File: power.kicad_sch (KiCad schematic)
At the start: 27 parts, among them IC1 SiC437BED-T1-GE3, J4 Barrel_Jack_Switch, Q1 PXP012-30QLJ, Q2 PXP012-30QLJ, U2 LTC4412xS6

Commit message: with ports for steppers
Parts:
- IC1: footprint SiC437BEDT1GE3 -> iclr:SiC437BEDT1GE3
- Q1, Q2: footprint PXP01230QLJ -> iclr:PXP01230QLJ
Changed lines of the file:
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@@
 			)
 		)
-		(property "Footprint" "PXP01230QLJ"
+		(property "Footprint" "iclr:PXP01230QLJ"
 			(at 96.52 88.9 0)
 			(effects
@@
 			)
 		)
-		(property "Footprint" "SiC437BEDT1GE3"
+		(property "Footprint" "iclr:SiC437BEDT1GE3"
 			(at 187.96 35.56 0)
 			(effects
@@
 			)
 		)
-		(property "Footprint" "PXP01230QLJ"
+		(property "Footprint" "iclr:PXP01230QLJ"
 			(at 81.28 21.59 0)
 			(effects

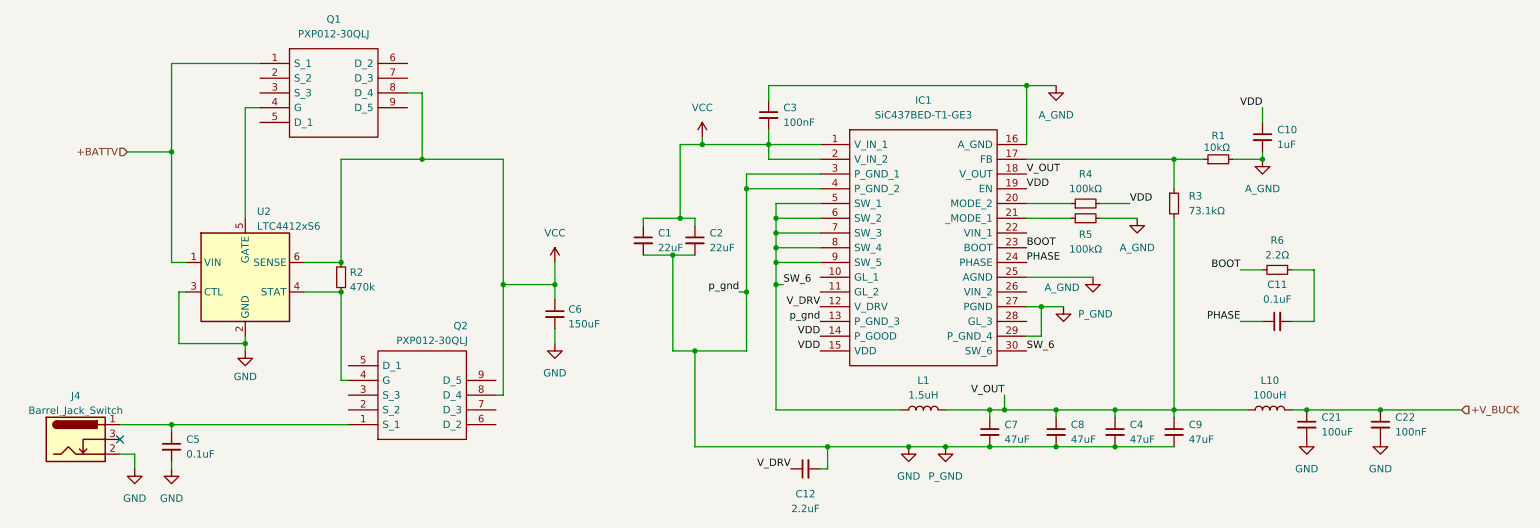
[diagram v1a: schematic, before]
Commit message: added zener diodes
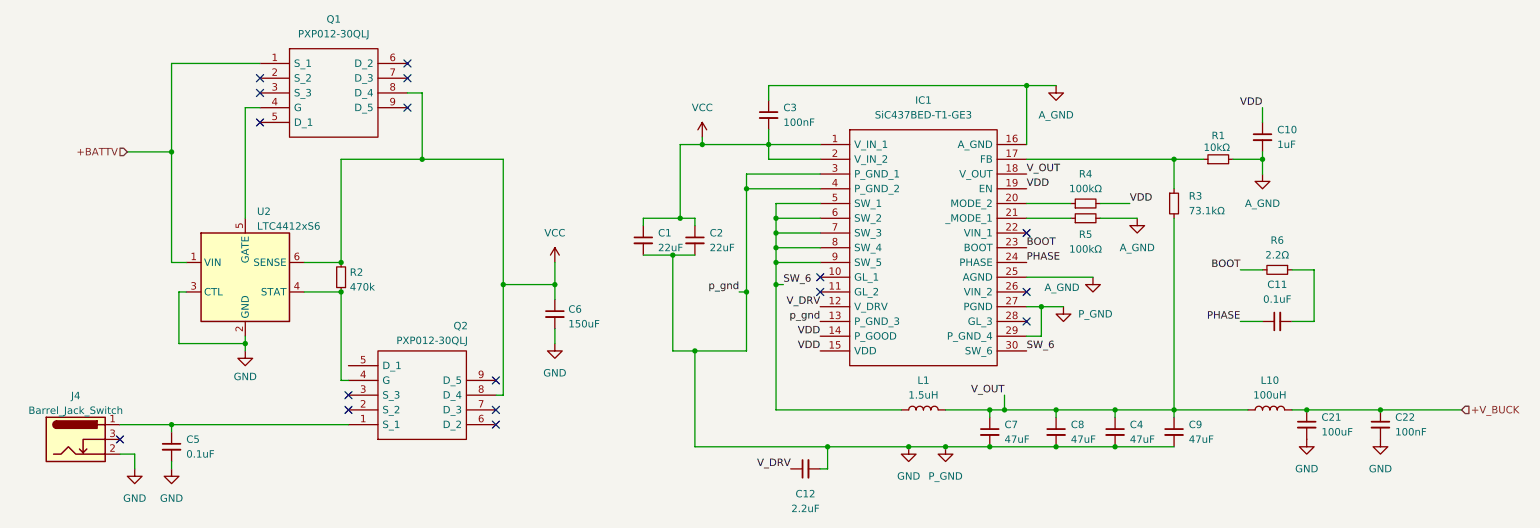
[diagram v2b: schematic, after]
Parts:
- C1, C2: footprint (none) -> Capacitor_SMD:C_0805_2012Metric
- C10, C12: footprint (none) -> Capacitor_SMD:C_0603_1608Metric
- C11, C22, C3: footprint (none) -> Capacitor_SMD:C_0402_1005Metric
- C21: footprint (none) -> Capacitor_SMD:C_Elec_6.3x5.4
- C4, C7, C8, C9: footprint (none) -> Capacitor_SMD:C_1206_3216Metric
- C5: footprint Capacitor_SMD:C_0603_1608Metric -> Capacitor_SMD:C_0402_1005Metric
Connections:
- no-connect marks 1 -> 17
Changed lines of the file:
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@@
 	)
 	(no_connect
+		(at 85.09 31.75)
+	)
+	(no_connect
+		(at 59.69 29.21)
+	)
+	(no_connect
+		(at 74.93 83.82)
+	)
+	(no_connect
+		(at 191.77 53.34)
+	)
+	(no_connect
+		(at 191.77 63.5)
+	)
+	(no_connect
 		(at 35.56 88.9)
 	)
+	(no_connect
+		(at 156.21 60.96)
+	)
+	(no_connect
+		(at 156.21 63.5)
+	)
+	(no_connect
+		(at 59.69 26.67)
+	)
+	(no_connect
+		(at 100.33 86.36)
+	)
+	(no_connect
+		(at 100.33 78.74)
+	)
+	(no_connect
+		(at 191.77 68.58)
+	)
+	(no_connect
+		(at 74.93 81.28)
+	)
+	(no_connect
+		(at 85.09 26.67)
+	)
+	(no_connect
+		(at 85.09 24.13)
+	)
+	(no_connect
+		(at 59.69 34.29)
+	)
+	(no_connect
+		(at 100.33 83.82)
+	)
 	(wire
 		(pts
@@
 	(wire
 		(pts
+			(xy 232.41 43.18) (xy 232.41 40.64)
+		)
+		(stroke
+			(width 0)
+			(type default)
+		)
+	)
+	(wire
+		(pts
 			(xy 148.59 58.42) (xy 148.59 62.23)
 		)
@@
 			)
 		)
-		(property "Footprint" ""
+		(property "Footprint" "Capacitor_SMD:C_Elec_6.3x5.4"
 			(at 240.03 86.36 0)
 			(effects
@@
 			)
 		)
-		(property "Footprint" ""
+		(property "Footprint" "Capacitor_SMD:C_0402_1005Metric"
 			(at 234.95 68.58 0)
 			(effects
@@
 			)
 		)
-		(property "Footprint" ""
+		(property "Footprint" "Capacitor_SMD:C_0603_1608Metric"
 			(at 153.67 93.98 0)
 			(effects
@@
 			)
 		)
-		(property "Footprint" ""
+		(property "Footprint" "Capacitor_SMD:C_1206_3216Metric"
 			(at 185.42 87.63 0)
 			(effects
@@
 			)
 		)
-		(property "Footprint" ""
+		(property "Footprint" "Capacitor_SMD:C_0805_2012Metric"
 			(at 125.73 54.61 0)
 			(effects
@@
 			)
 		)
-		(property "Footprint" ""
+		(property "Footprint" "Capacitor_SMD:C_0805_2012Metric"
 			(at 134.62 54.61 0)
 			(effects
@@
 			)
 		)
-		(property "Footprint" ""
+		(property "Footprint" "Capacitor_SMD:C_1206_3216Metric"
 			(at 207.01 87.63 0)
 			(effects
@@
 			)
 		)
-		(property "Footprint" ""
+		(property "Footprint" "Capacitor_SMD:C_0603_1608Metric"
 			(at 232.41 36.83 0)
 			(effects
@@
 			)
 		)
-		(property "Footprint" ""
+		(property "Footprint" "Capacitor_SMD:C_1206_3216Metric"
 			(at 217.17 87.63 0)
 			(effects
@@
 			)
 		)
-		(property "Footprint" ""
+		(property "Footprint" "Capacitor_SMD:C_1206_3216Metric"
 			(at 196.85 87.63 0)
 			(effects
@@
 			)
 		)
-		(property "Footprint" "Capacitor_SMD:C_0603_1608Metric"
+		(property "Footprint" "Capacitor_SMD:C_0402_1005Metric"
 			(at 44.45 90.17 0)
 			(effects
@@
 	(symbol
 		(lib_id "power:GND")
-		(at 232.41 40.64 0)
+		(at 232.41 43.18 0)
 		(unit 1)
 		(exclude_from_sim no)
@@
 		(fields_autoplaced yes)
 		(property "Reference" "#PWR06"
-			(at 232.41 46.99 0)
+			(at 232.41 49.53 0)
 			(effects
 				(font
@@
 		)
 		(property "Value" "A_GND"
-			(at 232.41 45.72 0)
+			(at 232.41 48.26 0)
 			(effects
 				(font
@@
 		)
 		(property "Footprint" ""
-			(at 232.41 40.64 0)
+			(at 232.41 43.18 0)
 			(effects
 				(font
@@
 		)
 		(property "Datasheet" ""
-			(at 232.41 40.64 0)
+			(at 232.41 43.18 0)
 			(effects
 				(font
@@
 		)
 		(property "Description" "Power symbol creates a global label with name \"GND\" , ground"
-			(at 232.41 40.64 0)
+			(at 232.41 43.18 0)
 			(effects
 				(font
@@
 			)
 		)
-		(property "Footprint" ""
+		(property "Footprint" "Capacitor_SMD:C_0402_1005Metric"
 			(at 147.32 33.02 0)
 			(effects
@@
 			)
 		)
-		(property "Footprint" ""
+		(property "Footprint" "Capacitor_SMD:C_0402_1005Metric"
 			(at 252.73 86.36 0)
 			(effects

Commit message: UPDATE
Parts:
- L1: footprint (none) -> Inductor_SMD:L_1008_2520Metric
- L10: footprint (none) -> iclr:SDR1307A101K
- R1: footprint (none) -> Resistor_SMD:R_0805_2012Metric
- R3: value 73.1kΩ -> 73.2kΩ; footprint (none) -> iclr:ERJHP6D1000V
- R4, R5: footprint (none) -> Resistor_SMD:R_2010_5025Metric_Pad1.40x2.65mm_HandSolder
- R6: footprint (none) -> Resistor_SMD:R_0603_1608Metric_Pad0.98x0.95mm_HandSolder
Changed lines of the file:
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@@
 			)
 		)
-		(property "Footprint" ""
+		(property "Footprint" "Resistor_SMD:R_0805_2012Metric"
 			(at 224.79 40.64 0)
 			(effects
@@
 			)
 		)
-		(property "Footprint" ""
+		(property "Footprint" "Resistor_SMD:R_0603_1608Metric_Pad0.98x0.95mm_HandSolder"
 			(at 234.95 59.69 0)
 			(effects
@@
 			)
 		)
-		(property "Footprint" ""
+		(property "Footprint" "Inductor_SMD:L_1008_2520Metric"
 			(at 173.99 83.82 0)
 			(effects
@@
 			)
 		)
-		(property "Value" "73.1kΩ"
+		(property "Value" "73.2kΩ"
 			(at 219.71 49.5299 0)
 			(effects
@@
 			)
 		)
-		(property "Footprint" ""
+		(property "Footprint" "iclr:ERJHP6D1000V"
 			(at 217.17 48.26 0)
 			(effects
@@
 			)
 		)
-		(property "Footprint" ""
+		(property "Footprint" "Resistor_SMD:R_2010_5025Metric_Pad1.40x2.65mm_HandSolder"
 			(at 201.93 50.8 0)
 			(effects
@@
 			)
 		)
-		(property "Footprint" ""
+		(property "Footprint" "Resistor_SMD:R_2010_5025Metric_Pad1.40x2.65mm_HandSolder"
 			(at 201.93 48.26 0)
 			(effects
@@
 			)
 		)
-		(property "Footprint" ""
+		(property "Footprint" "iclr:SDR1307A101K"
 			(at 233.68 83.82 0)
 			(effects

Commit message: update 2 everything is fixed
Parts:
- R4, R5: footprint Resistor_SMD:R_2010_5025Metric_Pad1.40x2.65mm_HandSolder -> Resistor_SMD:R_0402_1005Metric
- R6: footprint Resistor_SMD:R_0603_1608Metric_Pad0.98x0.95mm_HandSolder -> Resistor_SMD:R_0402_1005Metric
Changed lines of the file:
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@@
 			)
 		)
-		(property "Footprint" "Resistor_SMD:R_0603_1608Metric_Pad0.98x0.95mm_HandSolder"
+		(property "Footprint" "Resistor_SMD:R_0402_1005Metric"
 			(at 234.95 59.69 0)
 			(effects
@@
 			)
 		)
-		(property "Footprint" "Resistor_SMD:R_2010_5025Metric_Pad1.40x2.65mm_HandSolder"
+		(property "Footprint" "Resistor_SMD:R_0402_1005Metric"
 			(at 201.93 50.8 0)
 			(effects
@@
 			)
 		)
-		(property "Footprint" "Resistor_SMD:R_2010_5025Metric_Pad1.40x2.65mm_HandSolder"
+		(property "Footprint" "Resistor_SMD:R_0402_1005Metric"
 			(at 201.93 48.26 0)
 			(effects

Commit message: ideal diode update to be checked
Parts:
- removed J4: Barrel_Jack_Switch, Connector_BarrelJack:BarrelJack_Wuerth_6941xx301002, symbol Connector:Barrel_Jack_Switch
- added J3: XT60PW-M, iclr:AMASS_XT60PW-M, symbol ICLR:XT60PW-M
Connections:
- net +BATTV: now also C5.1, Q2.1 (S_1), J3.1 (+)
- net GND: now also J3.2 (-)
- no-connect marks 17 -> 16
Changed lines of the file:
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@@
 	)
 	(junction
+		(at 44.45 58.42)
+		(diameter 0)
+		(color 0 0 0 0)
+	)
+	(junction
 		(at 196.85 90.17)
 		(diameter 0)
@@
 	)
 	(no_connect
-		(at 35.56 88.9)
-	)
-	(no_connect
 		(at 156.21 60.96)
 	)
@@
 	(wire
 		(pts
+			(xy 44.45 58.42) (xy 44.45 86.36)
+		)
+		(stroke
+			(width 0)
+			(type default)
+		)
+	)
+	(wire
+		(pts
 			(xy 67.31 63.5) (xy 73.66 63.5)
 		)
@@
 	(wire
 		(pts
-			(xy 57.15 71.12) (xy 57.15 72.39)
+			(xy 34.29 87.63) (xy 34.29 86.36)
 		)
 		(stroke
@@
 	(wire
 		(pts
-			(xy 191.77 66.04) (xy 194.31 66.04)
+			(xy 57.15 71.12) (xy 57.15 72.39)
 		)
 		(stroke
@@
 	(wire
 		(pts
-			(xy 217.17 85.09) (xy 217.17 83.82)
+			(xy 191.77 66.04) (xy 194.31 66.04)
 		)
 		(stroke
@@
 	(wire
 		(pts
-			(xy 46.99 63.5) (xy 45.72 63.5)
+			(xy 34.29 90.17) (xy 34.29 91.44)
 		)
 		(stroke
@@
 	(wire
 		(pts
-			(xy 101.6 81.28) (xy 101.6 62.23)
+			(xy 217.17 85.09) (xy 217.17 83.82)
 		)
 		(stroke
@@
 	(wire
 		(pts
-			(xy 148.59 50.8) (xy 148.59 53.34)
+			(xy 101.6 81.28) (xy 101.6 62.23)
 		)
 		(stroke
@@
 	(wire
 		(pts
-			(xy 35.56 91.44) (xy 38.1 91.44)
+			(xy 148.59 50.8) (xy 148.59 53.34)
 		)
 		(stroke
@@
 	(wire
 		(pts
-			(xy 45.72 63.5) (xy 45.72 72.39)
+			(xy 46.99 63.5) (xy 46.99 72.39)
 		)
 		(stroke
@@
 	(wire
 		(pts
-			(xy 44.45 58.42) (xy 46.99 58.42)
+			(xy 187.96 83.82) (xy 196.85 83.82)
 		)
 		(stroke
@@
 	(wire
 		(pts
-			(xy 187.96 83.82) (xy 196.85 83.82)
+			(xy 241.3 68.58) (xy 241.3 59.69)
 		)
 		(stroke
@@
 	(wire
 		(pts
-			(xy 241.3 68.58) (xy 241.3 59.69)
+			(xy 185.42 90.17) (xy 196.85 90.17)
 		)
 		(stroke
@@
 	(wire
 		(pts
-			(xy 185.42 90.17) (xy 196.85 90.17)
+			(xy 147.32 35.56) (xy 147.32 38.1)
 		)
 		(stroke
@@
 	(wire
 		(pts
-			(xy 147.32 35.56) (xy 147.32 38.1)
+			(xy 143.51 63.5) (xy 143.51 73.66)
 		)
 		(stroke
@@
 	(wire
 		(pts
-			(xy 143.51 63.5) (xy 143.51 73.66)
+			(xy 67.31 58.42) (xy 73.66 58.42)
 		)
 		(stroke
@@
 	(wire
 		(pts
-			(xy 67.31 58.42) (xy 73.66 58.42)
+			(xy 34.29 86.36) (xy 44.45 86.36)
 		)
 		(stroke
@@
 	(wire
 		(pts
+			(xy 44.45 58.42) (xy 46.99 58.42)
+		)
+		(stroke
+			(width 0)
+			(type default)
+		)
+	)
+	(wire
+		(pts
 			(xy 87.63 40.64) (xy 101.6 40.64)
 		)
@@
 	(wire
 		(pts
-			(xy 45.72 72.39) (xy 57.15 72.39)
+			(xy 46.99 72.39) (xy 57.15 72.39)
 		)
 		(stroke
@@
 	(wire
 		(pts
-			(xy 35.56 86.36) (xy 44.45 86.36)
-		)
-		(stroke
-			(width 0)
-			(type default)
-		)
-	)
-	(wire
-		(pts
 			(xy 143.51 45.72) (xy 143.51 63.5)
 		)
@@
 	(wire
 		(pts
+			(xy 34.29 91.44) (xy 38.1 91.44)
+		)
+		(stroke
+			(width 0)
+			(type default)
+		)
+	)
+	(wire
+		(pts
 			(xy 132.08 50.8) (xy 132.08 38.1)
 		)
@@
 	)
 	(symbol
-		(lib_id "Connector:Barrel_Jack_Switch")
-		(at 27.94 88.9 0)
-		(unit 1)
-		(exclude_from_sim no)
-		(in_bom yes)
-		(on_board yes)
-		(dnp no)
-		(property "Reference" "J4"
-			(at 27.94 81.3902 0)
-			(effects
-				(font
-					(size 1.27 1.27)
-				)
-			)
-		)
-		(property "Value" "Barrel_Jack_Switch"
-			(at 27.94 83.9271 0)
-			(effects
-				(font
-					(size 1.27 1.27)
-				)
-			)
-		)
-		(property "Footprint" "Connector_BarrelJack:BarrelJack_Wuerth_6941xx301002"
-			(at 29.21 89.916 0)
-			(effects
-				(font
-					(size 1.27 1.27)
-				)
-				(hide yes)
-			)
-		)
-		(property "Datasheet" "~"
-			(at 29.21 89.916 0)
-			(effects
-				(font
-					(size 1.27 1.27)
-				)
-				(hide yes)
-			)
-		)
-		(property "Description" ""
-			(at 27.94 88.9 0)
-			(effects
-				(font
-					(size 1.27 1.27)
-				)
-				(hide yes)
-			)
-		)
-		(pin "1"
-		)
-		(pin "2"
-		)
-		(pin "3"
-		)
-		(instances
-			(project "BetetrDom"
-				(path "/3d73b00f-865e-402b-88ef-ae22e0a8ba36/837d0d5a-cb41-4001-b9fc-855d4a9018ff"
-					(reference "J4")
-					(unit 1)
-				)
-			)
-		)
-	)
-	(symbol
 		(lib_id "power:VCC")
 		(at 110.49 58.42 0)
@@
 					(unit 1)
 				)
+			)
+		)
+	)
+	(symbol
+		(lib_id "ICLR:XT60PW-M")
+		(at 24.13 90.17 0)
+		(mirror y)
+		(unit 1)
+		(exclude_from_sim no)
+		(in_bom yes)
+		(on_board yes)
+		(dnp no)
+		(property "Reference" "J3"
+			(at 24.13 97.79 0)
+			(effects
+				(font
+					(size 1.27 1.27)
+				)
+			)
+		)
+		(property "Value" "XT60PW-M"
+			(at 24.13 95.25 0)
+			(effects
+				(font
+					(size 1.27 1.27)
+				)
+			)
+		)
+		(property "Footprint" "iclr:AMASS_XT60PW-M"
+			(at 24.13 90.17 0)
+			(effects
+				(font
+					(size 1.27 1.27)
+				)
+				(justify bottom)
+				(hide yes)
+			)
+		)
+		(property "Datasheet" ""
+			(at 24.13 90.17 0)
+			(effects
+				(font
+					(size 1.27 1.27)
+				)
+				(hide yes)
+			)
+		)
+		(property "Description" ""
+			(at 24.13 90.17 0)
+			(effects
+				(font
+					(size 1.27 1.27)
+				)
+				(hide yes)
+			)
+		)
+		(property "STANDARD" "Manufacturer recommendations"
+			(at 24.13 90.17 0)
+			(effects
+				(font
+					(size 1.27 1.27)
+				)
+				(justify bottom)
+				(hide yes)
+			)
+		)
+		(property "MANUFACTURER" "AMASS"
+			(at 24.13 90.17 0)
+			(effects
+				(font
+					(size 1.27 1.27)
+				)
+				(justify bottom)
+				(hide yes)
+			)
+		)
+		(property "PARTREV" "V1.2"
+			(at 24.13 90.17 0)
+			(effects
+				(font
+					(size 1.27 1.27)
+				)
+				(justify bottom)
+				(hide yes)
+			)
+		)
+		(property "MAXIMUM_PACKAGE_HEIGHT" "8.4 mm"
+			(at 24.13 90.17 0)
+			(effects
+				(font
+					(size 1.27 1.27)
+				)
+				(justify bottom)
+				(hide yes)
+			)
+		)
+		(pin "1"
+		)
+		(pin "2"
+		)
+		(instances
+			(project "BetetrDom"
+				(path "/3d73b00f-865e-402b-88ef-ae22e0a8ba36/837d0d5a-cb41-4001-b9fc-855d4a9018ff"
+					(reference "J3")
+					(unit 1)
+				)

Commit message: update again
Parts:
- removed J3: XT60PW-M, iclr:AMASS_XT60PW-M, symbol ICLR:XT60PW-M
- added J4: XT60PW-M, iclr:AMASS_XT60PW-M, symbol ICLR:XT60PW-M
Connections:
- net +BATTV: no longer Q1.1 (S_1), U2.1 (VIN)
- net GND: now also J4.2 (-)
- new net: J4.1 (+), Q1.1 (S_1), U2.1 (VIN)

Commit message: update
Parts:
- removed C5: 0.1uF, Capacitor_SMD:C_0402_1005Metric, symbol Device:C_Small
- added C23: 0.1uF, Capacitor_SMD:C_0402_1005Metric, symbol Device:C_Small
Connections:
- net GND: now also C23.2; no longer J4.2 (-)
- new net: C23.1, J4.2 (-)
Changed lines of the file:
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@@
 	)
 	(junction
-		(at 44.45 86.36)
-		(diameter 0)
-		(color 0 0 0 0)
-	)
-	(junction
 		(at 110.49 62.23)
 		(diameter 0)
@@
 	(wire
 		(pts
-			(xy 30.48 86.36) (xy 44.45 86.36)
-		)
-		(stroke
-			(width 0)
-			(type default)
-		)
-	)
-	(wire
-		(pts
 			(xy 148.59 48.26) (xy 148.59 50.8)
 		)
@@
 	(wire
 		(pts
+			(xy 36.83 50.8) (xy 36.83 49.53)
+		)
+		(stroke
+			(width 0)
+			(type default)
+		)
+	)
+	(wire
+		(pts
 			(xy 44.45 58.42) (xy 46.99 58.42)
 		)
@@
 	(wire
 		(pts
-			(xy 44.45 86.36) (xy 74.93 86.36)
+			(xy 30.48 86.36) (xy 74.93 86.36)
 		)
 		(stroke
@@
 	(wire
 		(pts
-			(xy 44.45 92.71) (xy 44.45 93.98)
+			(xy 191.77 71.12) (xy 194.31 71.12)
 		)
 		(stroke
@@
 	(wire
 		(pts
-			(xy 191.77 71.12) (xy 194.31 71.12)
+			(xy 36.83 44.45) (xy 36.83 41.91)
 		)
 		(stroke
@@
 	(wire
 		(pts
-			(xy 44.45 86.36) (xy 44.45 87.63)
-		)
-		(stroke
-			(width 0)
-			(type default)
-		)
-	)
-	(wire
-		(pts
 			(xy 110.49 62.23) (xy 110.49 64.77)
 		)
@@
 	(symbol
 		(lib_id "power:GND")
-		(at 36.83 41.91 0)
+		(at 36.83 50.8 0)
 		(unit 1)
 		(exclude_from_sim no)
@@
 		(fields_autoplaced yes)
 		(property "Reference" "#PWR041"
-			(at 36.83 48.26 0)
+			(at 36.83 57.15 0)
 			(effects
 				(font
@@
 		)
 		(property "Value" "GND"
-			(at 36.83 46.99 0)
+			(at 36.83 55.88 0)
 			(effects
 				(font
@@
 		)
 		(property "Footprint" ""
-			(at 36.83 41.91 0)
+			(at 36.83 50.8 0)
 			(effects
 				(font
@@
 		)
 		(property "Datasheet" ""
-			(at 36.83 41.91 0)
+			(at 36.83 50.8 0)
 			(effects
 				(font
@@
 		)
 		(property "Description" "Power symbol creates a global label with name \"GND\" , ground"
-			(at 36.83 41.91 0)
+			(at 36.83 50.8 0)
 			(effects
 				(font
@@
 	)
 	(symbol
+		(lib_id "Device:C_Small")
+		(at 36.83 46.99 0)
+		(unit 1)
+		(exclude_from_sim no)
+		(in_bom yes)
+		(on_board yes)
+		(dnp no)
+		(fields_autoplaced yes)
+		(property "Reference" "C23"
+			(at 39.37 45.7262 0)
+			(effects
+				(font
+					(size 1.27 1.27)
+				)
+				(justify left)
+			)
+		)
+		(property "Value" "0.1uF"
+			(at 39.37 48.2662 0)
+			(effects
+				(font
+					(size 1.27 1.27)
+				)
+				(justify left)
+			)
+		)
+		(property "Footprint" "Capacitor_SMD:C_0402_1005Metric"
+			(at 36.83 46.99 0)
+			(effects
+				(font
+					(size 1.27 1.27)
+				)
+				(hide yes)
+			)
+		)
+		(property "Datasheet" "~"
+			(at 36.83 46.99 0)
+			(effects
+				(font
+					(size 1.27 1.27)
+				)
+				(hide yes)
+			)
+		)
+		(property "Description" "Unpolarized capacitor, small symbol"
+			(at 36.83 46.99 0)
+			(effects
+				(font
+					(size 1.27 1.27)
+				)
+				(hide yes)
+			)
+		)
+		(pin "1"
+		)
+		(pin "2"
+		)
+		(instances
+			(project ""
+				(path "/3d73b00f-865e-402b-88ef-ae22e0a8ba36/837d0d5a-cb41-4001-b9fc-855d4a9018ff"
+					(reference "C23")
+					(unit 1)
+				)
+			)
+		)
+	)
+	(symbol
 		(lib_id "Device:R_Small")
 		(at 201.93 50.8 90)
@@
 					(unit 1)
 				)
-			)
-		)
-	)
-	(symbol
-		(lib_id "Device:C_Small")
-		(at 44.45 90.17 0)
-		(unit 1)
-		(exclude_from_sim no)
-		(in_bom yes)
-		(on_board yes)
-		(dnp no)
-		(fields_autoplaced yes)
-		(property "Reference" "C5"
-			(at 46.99 88.9062 0)
-			(effects
-				(font
-					(size 1.27 1.27)
-				)
-				(justify left)
-			)
-		)
-		(property "Value" "0.1uF"
-			(at 46.99 91.4462 0)
-			(effects
-				(font
-					(size 1.27 1.27)
-				)
-				(justify left)
-			)
-		)
-		(property "Footprint" "Capacitor_SMD:C_0402_1005Metric"
-			(at 44.45 90.17 0)
-			(effects
-				(font
-					(size 1.27 1.27)
-				)
-				(hide yes)
-			)
-		)
-		(property "Datasheet" "~"
-			(at 44.45 90.17 0)
-			(effects
-				(font
-					(size 1.27 1.27)
-				)
-				(hide yes)
-			)
-		)
-		(property "Description" ""
-			(at 44.45 90.17 0)
-			(effects
-				(font
-					(size 1.27 1.27)
-				)
-				(hide yes)
-			)
-		)
-		(pin "1"
-		)
-		(pin "2"
-		)
-		(instances
-			(project "BetetrDom"
-				(path "/3d73b00f-865e-402b-88ef-ae22e0a8ba36/837d0d5a-cb41-4001-b9fc-855d4a9018ff"
-					(reference "C5")
-					(unit 1)
-				)
-			)
-		)
-	)
-	(symbol
-		(lib_id "power:GND")
-		(at 44.45 93.98 0)
-		(unit 1)
-		(exclude_from_sim no)
-		(in_bom yes)
-		(on_board yes)
-		(dnp no)
-		(fields_autoplaced yes)
-		(property "Reference" "#PWR013"
-			(at 44.45 100.33 0)
-			(effects
-				(font
-					(size 1.27 1.27)
-				)
-				(hide yes)
-			)
-		)
-		(property "Value" "GND"
-			(at 44.45 99.06 0)
-			(effects
-				(font
-					(size 1.27 1.27)
-				)
-			)
-		)
-		(property "Footprint" ""
-			(at 44.45 93.98 0)
-			(effects
-				(font
-					(size 1.27 1.27)
-				)
-				(hide yes)
-			)
-		)
-		(property "Datasheet" ""
-			(at 44.45 93.98 0)
-			(effects
-				(font
-					(size 1.27 1.27)
-				)
-				(hide yes)
-			)
-		)
-		(property "Description" ""
-			(at 44.45 93.98 0)
-			(effects
-				(font
-					(size 1.27 1.27)
-				)
-				(hide yes)
-			)
-		)
-		(pin "1"
-		)
-		(instances
-			(project "BetetrDom"
-				(path "/3d73b00f-865e-402b-88ef-ae22e0a8ba36/837d0d5a-cb41-4001-b9fc-855d4a9018ff"
-					(reference "#PWR013")
-					(unit 1)
-				)

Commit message: finished pcb layouts, ready for check p sure
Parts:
- C10, C12: footprint Capacitor_SMD:C_0603_1608Metric -> Capacitor_SMD:C_0402_1005Metric
- R1: footprint Resistor_SMD:R_0805_2012Metric -> Resistor_SMD:R_0402_1005Metric
- R3: footprint iclr:ERJHP6D1000V -> Resistor_SMD:R_1206_3216Metric
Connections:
- net A_GND is gone; now on net GND: C10.2, C3.1, IC1.16 (A_GND), IC1.25 (AGND), R1.2, R5.2
- net VIN: now reaches IC1.22 (VIN_1)
- net VIN: now also IC1.26 (VIN_2)
- net SW_6 renamed SW
- net VCC renamed VMAIN
- no-connect marks 16 -> 15
